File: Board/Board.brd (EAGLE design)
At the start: 100 x 60 mm, 95 parts, among them Q1 SP0503BAHTG

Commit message: added OSHW Logo
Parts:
- added U$3: (no value), SparkFun-Aesthetics:OSHW-LOGO-L
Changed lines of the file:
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@@
 <attribute name="VALUE" x="42.905" y="42.675" size="1.27" layer="27" rot="R180"/>
 </element>
+<element name="U$3" library="SparkFun-Aesthetics" package="OSHW-LOGO-L" value="" x="5" y="7" rot="R270"/>
 </elements>
 <signals>

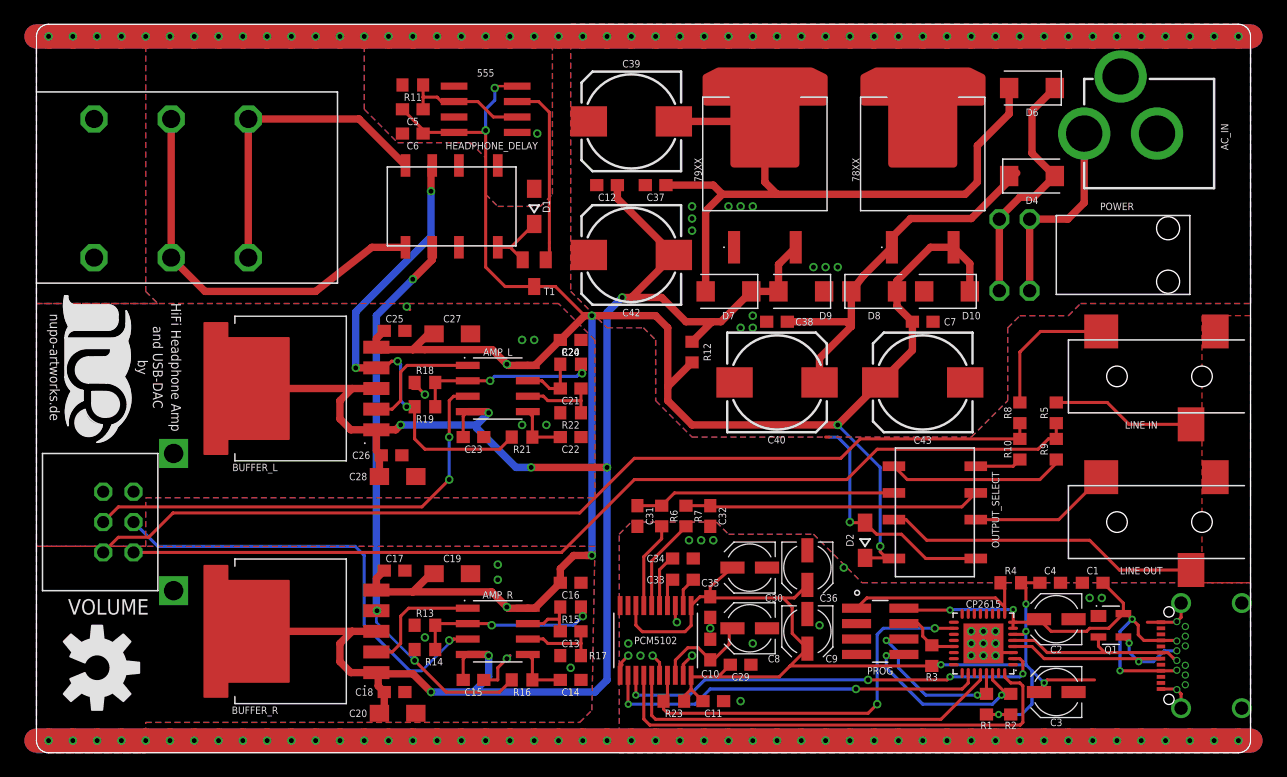
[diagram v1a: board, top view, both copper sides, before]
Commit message: fixed relay orientation to face powersupply
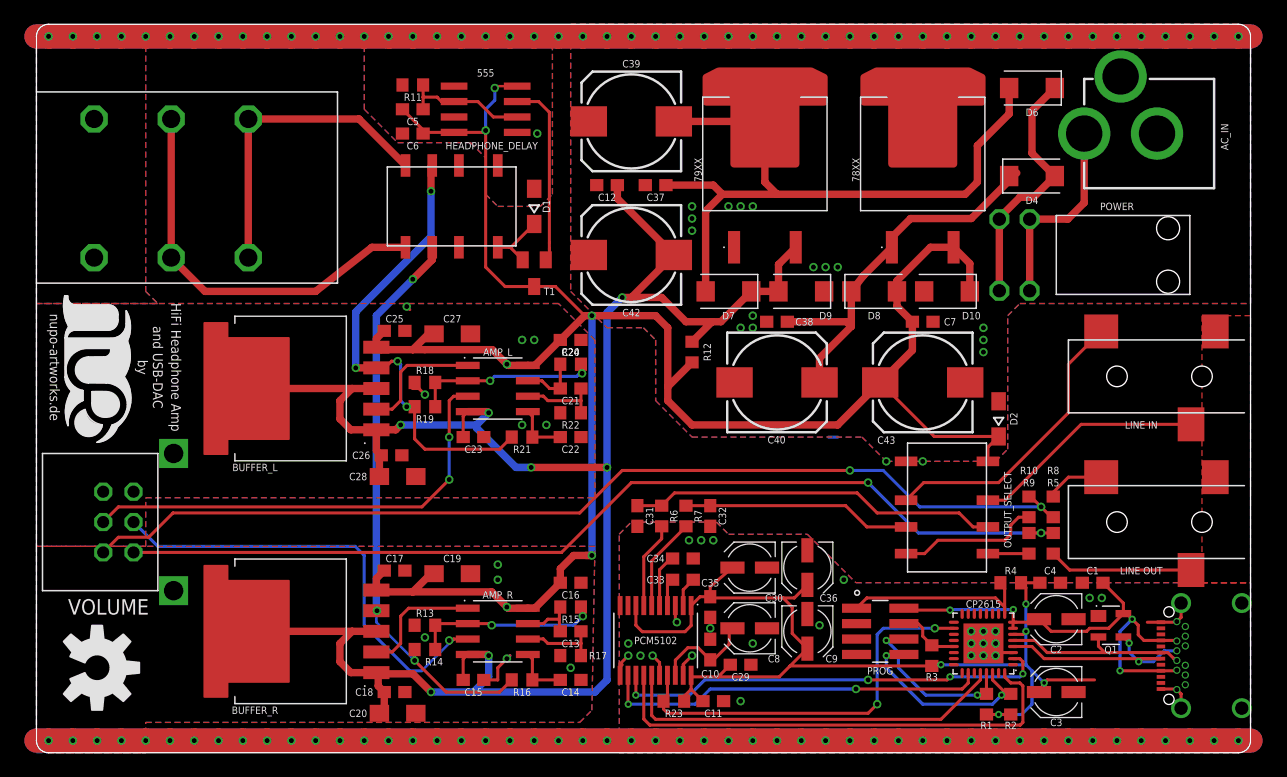
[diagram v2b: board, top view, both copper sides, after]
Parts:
- moved D2 14.9 mm to (79.2, 27.5)
- moved LINE_IN 12.0 mm to (99.5, 19.0)
- moved LINE_OUT 12.0 mm to (99.5, 31.0)
- moved R5 10.8 mm to (83.8, 17.2), turned to 270 degrees
- moved R8 8.22 mm to (83.8, 20.2)
- moved R9 8.07 mm to (81.8, 17.2)
- moved OUTPUT_SELECT 8.06 mm to (75.0, 24.0), turned to 270 degrees
- moved R10 4.81 mm to (81.8, 20.2)
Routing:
- net GND: track 446.5 -> 427.2 mm, vias 150 -> 154
- net N$20: track 11.8 -> 24.2 mm
- net N$37: track 14.7 -> 3.38 mm
- net R_LL: track 21.6 -> 30.5 mm
- net N$36: track 3.86 -> 11.8 mm
- net N$14: track 26.2 -> 19.3 mm
- net N$35: track 11.6 -> 4.82 mm
- net L_LL: track 24.6 -> 19.0 mm
- net AMP_IN_L: track 80.7 -> 84.4 mm, vias 0 -> 2
- net V+: track 175.8 -> 174.8 mm, vias 8 -> 6
- net AMP_IN_R: track 81.2 -> 80.9 mm, vias 0 -> 2

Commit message: fixed overlayp
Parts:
- moved C29 12.0 mm to (49.0, 15.2), turned to 270 degrees
- moved C8 1.00 mm to (58.8, 9.25)
- moved C9 0.75 mm to (63.5, 9.25)
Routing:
- net +3V3: track 87.6 -> 90.5 mm
- net GND: vias 154 -> 156
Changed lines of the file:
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@@
 <attribute name="VALUE" x="46.9226" y="9.25" size="1.27" layer="27" rot="R270" align="top-center"/>
 </element>
-<element name="C8" library="rcl" library_urn="urn:adsk.eagle:library:334" package="UD-4X5,8_NICHICON" package3d_urn="urn:adsk.eagle:package:23474/1" value="10µ" x="58.75" y="10.25" smashed="yes" rot="R180">
-<attribute name="NAME" x="60.75" y="7.75" size="0.6096" layer="25" rot="R180" align="center"/>
-<attribute name="SPICEPREFIX" value="C" x="58.75" y="10.25" size="1.778" layer="27" rot="R180" display="off"/>
-<attribute name="VALUE" x="60.655" y="13.425" size="1.016" layer="27" rot="R180"/>
-</element>
-<element name="C9" library="rcl" library_urn="urn:adsk.eagle:library:334" package="UD-4X5,8_NICHICON" package3d_urn="urn:adsk.eagle:package:23474/1" value="10µ" x="63.5" y="10" smashed="yes" rot="R270">
-<attribute name="NAME" x="65.5" y="7.75" size="0.6096" layer="25" rot="R180" align="center"/>
-<attribute name="SPICEPREFIX" value="C" x="63.5" y="10" size="1.778" layer="27" rot="R270" display="off"/>
-<attribute name="VALUE" x="60.325" y="11.905" size="1.016" layer="27" rot="R270"/>
+<element name="C8" library="rcl" library_urn="urn:adsk.eagle:library:334" package="UD-4X5,8_NICHICON" package3d_urn="urn:adsk.eagle:package:23474/1" value="10µ" x="58.75" y="9.25" smashed="yes" rot="R180">
+<attribute name="NAME" x="60.75" y="6.75" size="0.6096" layer="25" rot="R180" align="center"/>
+<attribute name="SPICEPREFIX" value="C" x="58.75" y="9.25" size="1.778" layer="27" rot="R180" display="off"/>
+<attribute name="VALUE" x="60.655" y="12.425" size="1.016" layer="27" rot="R180"/>
+</element>
+<element name="C9" library="rcl" library_urn="urn:adsk.eagle:library:334" package="UD-4X5,8_NICHICON" package3d_urn="urn:adsk.eagle:package:23474/1" value="10µ" x="63.5" y="9.25" smashed="yes" rot="R270">
+<attribute name="NAME" x="61.75" y="11.75" size="0.6096" layer="25" rot="R180" align="center"/>
+<attribute name="SPICEPREFIX" value="C" x="63.5" y="9.25" size="1.778" layer="27" rot="R270" display="off"/>
+<attribute name="VALUE" x="60.325" y="11.155" size="1.016" layer="27" rot="R270"/>
 </element>
 <element name="C10" library="rcl" library_urn="urn:adsk.eagle:library:334" package="C0603" package3d_urn="urn:adsk.eagle:package:23616/2" value="100n" x="55.5" y="8.5" smashed="yes" rot="R90">
@@
 <attribute name="VALUE" x="56.385" y="6.155" size="1.27" layer="27" rot="R180"/>
 </element>
-<element name="C29" library="rcl" library_urn="urn:adsk.eagle:library:334" package="C0603" package3d_urn="urn:adsk.eagle:package:23616/2" value="100n" x="58" y="7.25" smashed="yes" rot="R180">
-<attribute name="NAME" x="58" y="6.25" size="0.6096" layer="25" align="center"/>
-<attribute name="SPICEPREFIX" value="C" x="58" y="7.25" size="1.778" layer="27" rot="R180" display="off"/>
-<attribute name="VALUE" x="58.635" y="9.155" size="1.27" layer="27" rot="R180"/>
+<element name="C29" library="rcl" library_urn="urn:adsk.eagle:library:334" package="C0603" package3d_urn="urn:adsk.eagle:package:23616/2" value="100n" x="49" y="15.25" smashed="yes" rot="R270">
+<attribute name="NAME" x="49" y="17" size="0.6096" layer="25" rot="R180" align="center"/>
+<attribute name="SPICEPREFIX" value="C" x="49" y="15.25" size="1.778" layer="27" rot="R270" display="off"/>
+<attribute name="VALUE" x="47.095" y="15.885" size="1.27" layer="27" rot="R270"/>
 </element>
 <element name="C30" library="rcl" library_urn="urn:adsk.eagle:library:334" package="UD-4X5,8_NICHICON" package3d_urn="urn:adsk.eagle:package:23474/1" value="10µ" x="58.75" y="15.25" smashed="yes" rot="R180">
@@
 <via x="78" y="34" extent="1-16" drill="0.4" shape="octagon"/>
 <via x="78" y="35" extent="1-16" drill="0.4" shape="octagon"/>
+<via x="50.25" y="17.5" extent="1-16" drill="0.4" shape="octagon"/>
+<via x="48.25" y="17.75" extent="1-16" drill="0.4" shape="octagon"/>
 </signal>
 <signal name="+3V3">
@@
 <wire x1="49.375" y1="12.1217" x2="49.375" y2="10.5" width="0.254" layer="1"/>
 <wire x1="73.75" y1="7.15" x2="73.35" y2="6.75" width="0.254" layer="1"/>
-<wire x1="61.175" y1="6.25" x2="56.15" y2="6.25" width="0.254" layer="1"/>
-<wire x1="56.15" y1="6.25" x2="54" y2="6.25" width="0.254" layer="1"/>
+<wire x1="67.175" y1="6.25" x2="61.175" y2="6.25" width="0.254" layer="1"/>
 <wire x1="53.925" y1="12.1217" x2="53.925" y2="10.475" width="0.254" layer="1"/>
 <wire x1="82.575" y1="5" x2="83" y2="5.75" width="0.254" layer="1"/>
@@
 <wire x1="57.325" y1="15.25" x2="55.5" y2="13.675" width="0.254" layer="1"/>
 <wire x1="55.5" y1="13.675" x2="55.5" y2="12.85" width="0.254" layer="1"/>
-<wire x1="63.5" y1="8.575" x2="62.075" y2="7.15" width="0.254" layer="1"/>
-<wire x1="62.075" y1="7.15" x2="61.175" y2="6.25" width="0.254" layer="1"/>
+<wire x1="68.075" y1="7.15" x2="67.175" y2="6.25" width="0.254" layer="1"/>
 <wire x1="63.5" y1="13.825" x2="62.425" y2="12.75" width="0.254" layer="1"/>
 <wire x1="62.425" y1="12.75" x2="61.5" y2="12.75" width="0.254" layer="1"/>
 <wire x1="61.5" y1="12.75" x2="55.6" y2="12.75" width="0.254" layer="1"/>
-<wire x1="57.15" y1="7.25" x2="56.15" y2="6.25" width="0.254" layer="1"/>
-<wire x1="73.75" y1="7.15" x2="62.075" y2="7.15" width="0.254" layer="1"/>
-<wire x1="63.5" y1="8.575" x2="62.25" y2="9.825" width="0.254" layer="1"/>
-<wire x1="62.25" y1="9.825" x2="62.25" y2="12" width="0.254" layer="1"/>
+<wire x1="73.75" y1="7.15" x2="68.075" y2="7.15" width="0.254" layer="1"/>
 <wire x1="62.25" y1="12" x2="61.5" y2="12.75" width="0.254" layer="1"/>
 <wire x1="82.65" y1="14" x2="81.1" y2="14" width="0.254" layer="1"/>
+<wire x1="62.25" y1="12" x2="62.25" y2="7.325" width="0.254" layer="1"/>
+<wire x1="62.25" y1="7.325" x2="61.175" y2="6.25" width="0.254" layer="1"/>
+<wire x1="53.925" y1="6.3783" x2="54.0533" y2="6.25" width="0.254" layer="1"/>
+<wire x1="54.0533" y1="6.25" x2="61.175" y2="6.25" width="0.254" layer="1"/>
+<wire x1="49.375" y1="12.1217" x2="49.375" y2="14.025" width="0.254" layer="1"/>
+<wire x1="49.375" y1="14.025" x2="49" y2="14.4" width="0.254" layer="1"/>
+<wire x1="63.5" y1="7.825" x2="63" y2="7.325" width="0.254" layer="1"/>
+<wire x1="63" y1="7.325" x2="62.25" y2="7.325" width="0.254" layer="1"/>
 </signal>
 <signal name="N$10">
@@
 <wire x1="54.5" y1="8.65" x2="53.65" y2="8.65" width="0.254" layer="1"/>
 <wire x1="55.775" y1="7.65" x2="57.0625" y2="8.9375" width="0.254" layer="1"/>
-<wire x1="57.325" y1="10.25" x2="57.0625" y2="9.9875" width="0.254" layer="1"/>
+<wire x1="57.325" y1="9.25" x2="57.0625" y2="9.9875" width="0.254" layer="1"/>
 <wire x1="57.0625" y1="9.9875" x2="57.0625" y2="8.9375" width="0.254" layer="1"/>
 </signal>
